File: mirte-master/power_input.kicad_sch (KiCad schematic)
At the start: 3 parts, among them J20 sc, J22 sc, J7 INA226

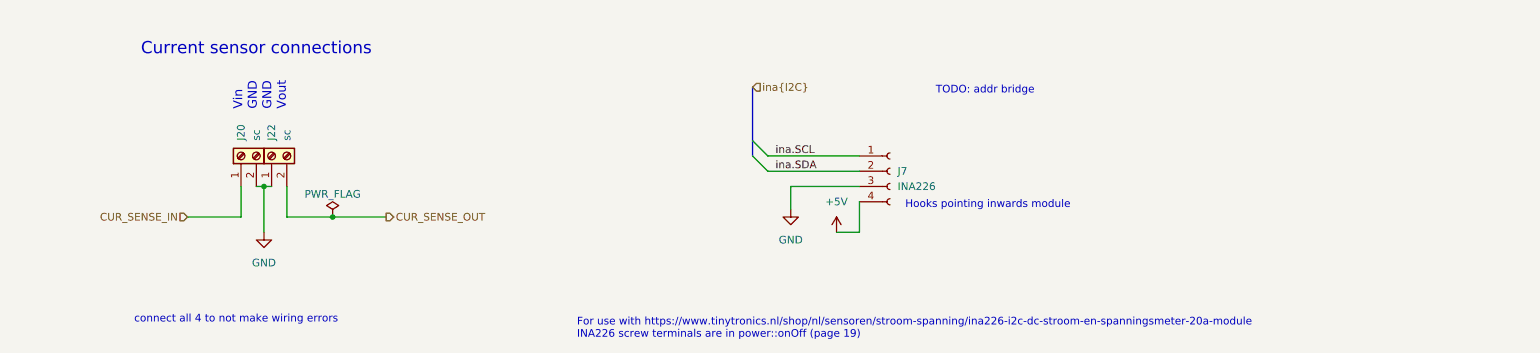
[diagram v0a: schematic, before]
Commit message: mirte-master schematic cleanup and readabilityimprovements
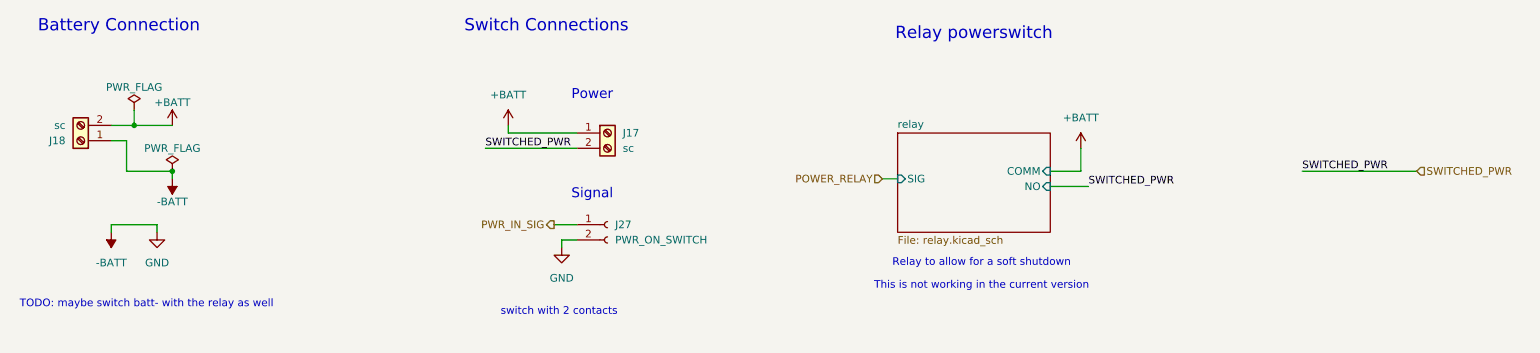
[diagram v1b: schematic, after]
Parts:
- removed J20, J22: sc, easyeda:CONN-TH_XY126V-5.0-2P, symbol Connector:Screw_Terminal_01x02
- removed J7: INA226, Connector_JST:JST_XH_B4B-XH-A_1x04_P2.50mm_Vertical, symbol Connector:Conn_01x04_Socket
- added J17, J18: sc, easyeda:CONN-TH_XY126V-5.0-2P, symbol Connector:Screw_Terminal_01x02
- added J27: PWR_ON_SWITCH, Connector_JST:JST_XH_B2B-XH-A_1x02_P2.50mm_Vertical, symbol Connector:Conn_01x02_Socket
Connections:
- new net +BATT: J17.1 (Pin_1), J18.2 (Pin_2)
- new net -BATT: J18.1 (Pin_1), J27.2 (Pin_2)
- new net PWR_IN_SIG: J27.1 (Pin_1)
- new net SWITCHED_PWR: J17.2 (Pin_2)
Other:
- added sheet relay (relay.kicad_sch)
- note added: "Battery Connection"
- note added: "Power"
- note added: "Relay powerswitch"
- note added: "Relay to allow for a soft shutdown"
- note added: "Signal"
- note added: "Switch Connections"
- note added: "TODO: maybe switch batt- with the relay as well"
- note added: "This is not working in the current version"
- note added: "switch with 2 contacts"
- note removed: "Current sensor connections"
- note removed: "For use with https://www.tinytronics.nl/shop/nl/sensoren/stroom-spanning/ina226-i2c-dc-stroom-en-spanningsmeter-20a-module INA226 screw terminals are in power::onOff (page 19)"
- note removed: "Hooks pointing inwards module"
- note removed: "TODO: addr bridge"
- note removed: "Vin GND GND Vout"
- note removed: "connect all 4 to not make wiring errors"
